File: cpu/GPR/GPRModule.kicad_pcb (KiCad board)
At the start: 2 copper layers, 100 x 80 mm, 51 parts, among them J1 Interconnect, U1 74HCT574, U10 74HCT245, U11 74HCT125, U2 74HCT574, U3 74HCT245, U4 74HCT245, U5 74HCT245, U6 74HCT245, U7 74HCT245, U8 74HCT245, U9 74HCT245

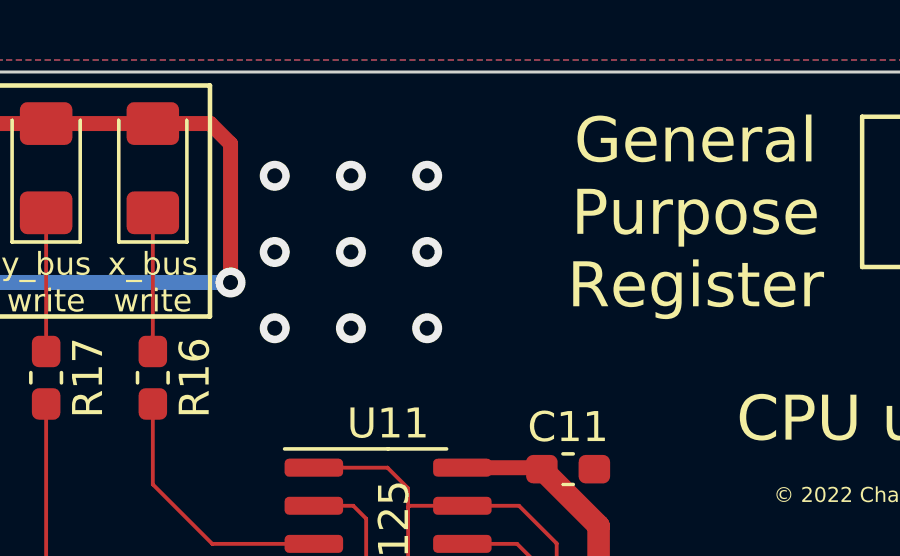
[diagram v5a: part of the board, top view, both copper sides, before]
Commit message: GPR 1.4, smaller traces and fixed connections being backwards
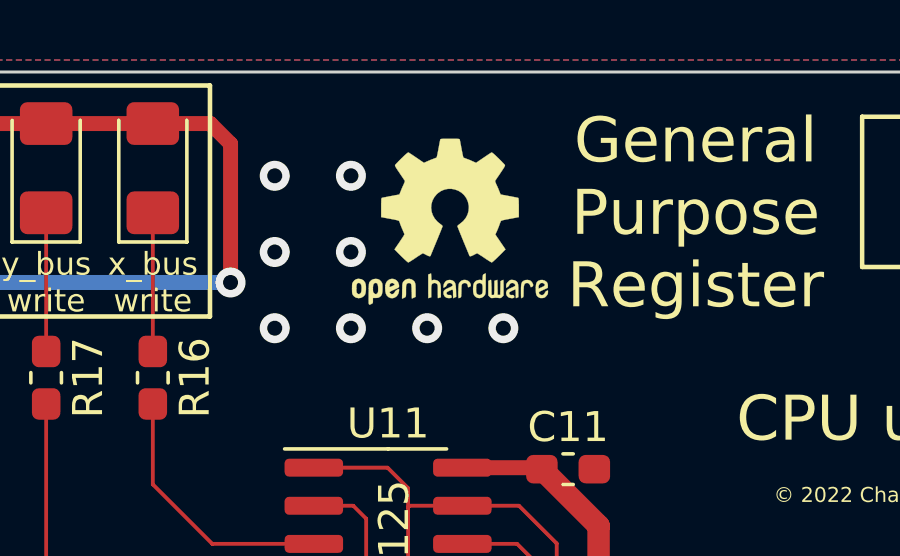
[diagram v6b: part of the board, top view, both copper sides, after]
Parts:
- added REF**: OSHW-Logo2_7.3x6mm_SilkScreen, Symbol:OSHW-Logo2_7.3x6mm_SilkScreen, F.Cu at (172.2, 62.5)
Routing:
- net GND: vias 111 -> 110
